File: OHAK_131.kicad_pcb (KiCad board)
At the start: 4 copper layers, 38.1 x 25.4 mm, 52 parts, among them P1 CONN_01X08, P2 USB_OTG, U1 rfd_77101, U2 MAX30100, U3 MIC5365-X.XYMT-TZ, U4 BMI160, U5 MCP73831, U6 MIC5365-X.XYMT-TZ, U7 TXS0102_LEVEL_SHIFTER_X2SON8, U8 MAX809

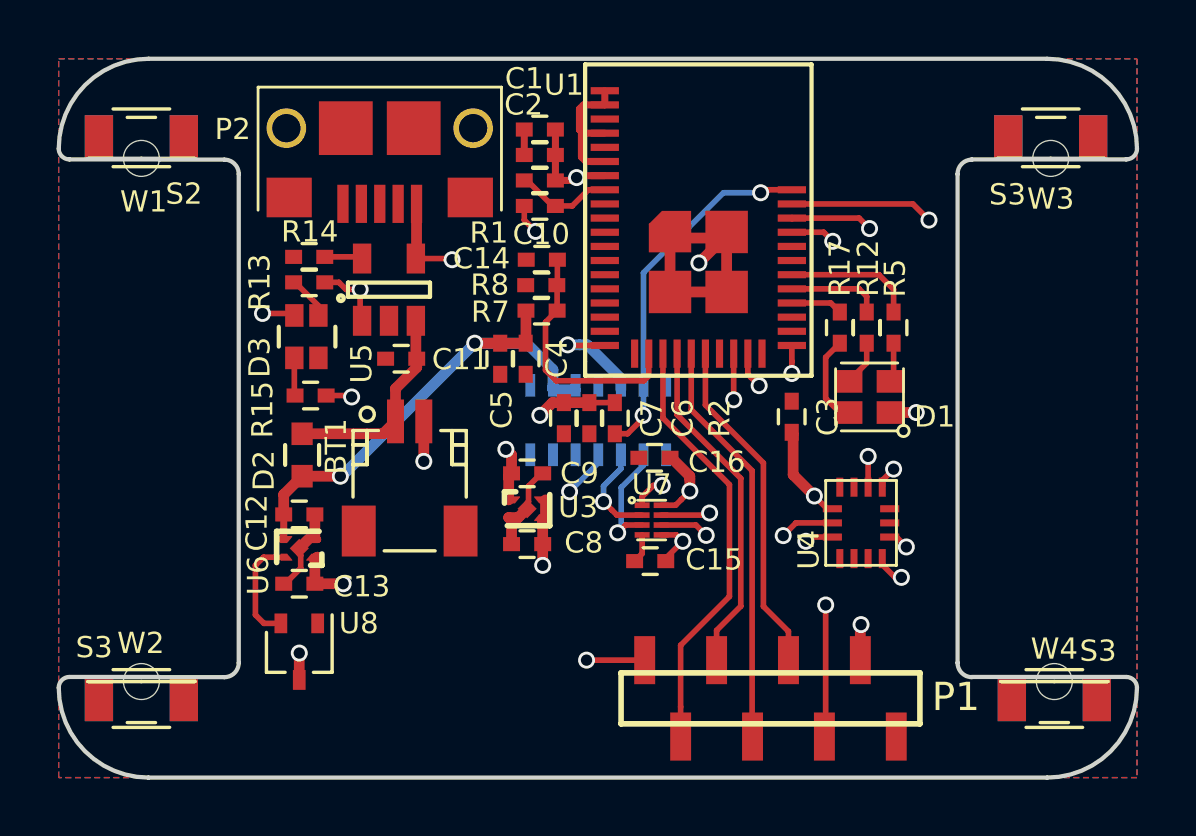
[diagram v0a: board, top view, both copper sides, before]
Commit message: fixed mis pinned part. moved stuff around
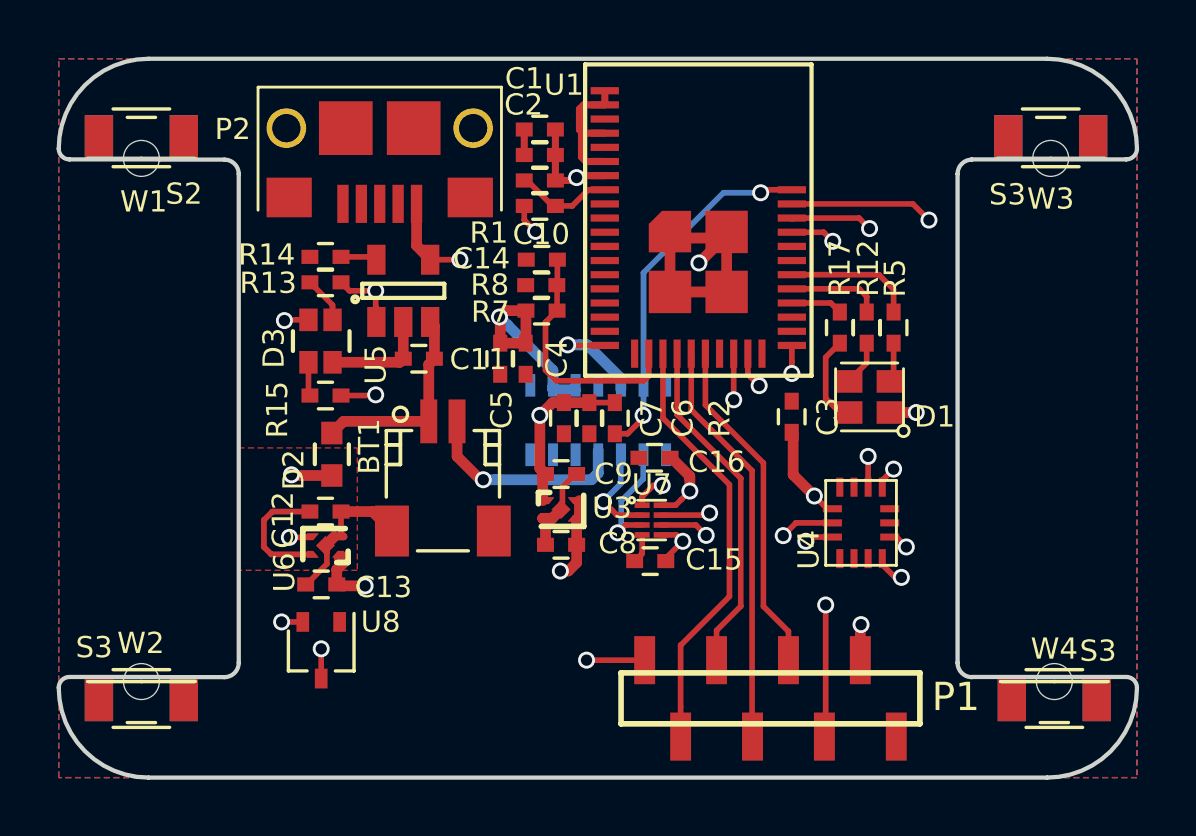
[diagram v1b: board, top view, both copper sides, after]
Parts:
- D1: value Led_RGB_CA -> ASMB-KTF0-0A306
- D3: value Dialight_R_G_LED -> 18-225SURSYGC/S530-A4/E4/TR8
- P1: value CONN_01X08 -> M50-3140845
- R12, R17: value 30R -> 100R
- R5: value 130R -> 100R
- U3: value MIC5365-X.XYMT-TZ -> MIC5365-1.8YMT-TZ
- U5: value MCP73831 -> MCP73831T-2ATI/OT
- U6: value MIC5365-X.XYMT-TZ -> MIC5365-3.0YMT-TZ
- U7: value TXS0102_LEVEL_SHIFTER_X2SON8 -> TXS0102DQER
- U8: value MAX809 -> MAX809SQ308T1G
- moved U3 1.20 mm to (139.1, 101.4)
- moved C8 1.20 mm to (139.1, 102.7)
- moved C9 1.20 mm to (139.1, 100.2)
- moved BT1 1.17 mm to (134.9, 100.2)
- moved D2 1.05 mm to (131.0, 99.5)
- moved C12 0.93 mm to (130.8, 101.5)
- moved U6 0.93 mm to (130.8, 102.7)
- moved U8 0.78 mm to (130.6, 106.4)
- moved C13 0.78 mm to (130.6, 104.1)
- moved C11 0.62 mm to (134.1, 96.1)
- moved R13 0.58 mm to (130.8, 93.4)
- moved R14 0.58 mm to (130.8, 92.5)
- moved R15 0.53 mm to (130.8, 97.4)
- moved D3 0.52 mm to (130.6, 95.5)
- moved U5 0.51 mm to (133.5, 93.7)
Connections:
- U6 pad 3: VPP -> /EN
- U6 pad 4: /EN -> VPP
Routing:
- net GND: track 33.4 -> 44.0 mm, vias 5 -> 4
- net VPP: track 26.1 -> 31.4 mm
- net +1V8: track 7.73 -> 8.96 mm, vias 4 -> 3
- net VDD: track 17.8 -> 18.9 mm
- net Net-(D3-Pad3): track 11.9 -> 11.2 mm
- net /EN: track 3.79 -> 4.49 mm, vias 0 -> 2
- added copper zone on F.Cu, net VPP

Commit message: FIXED BREAKS IN COPPER POURS
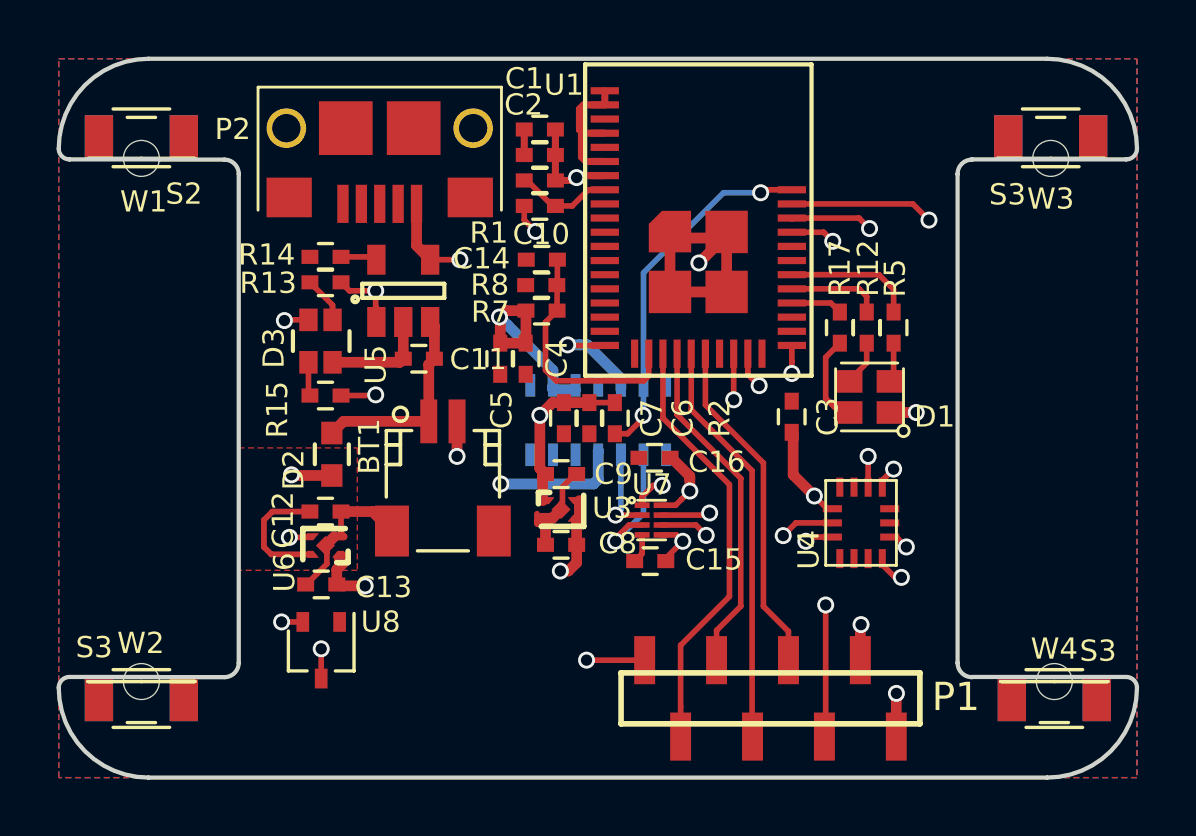
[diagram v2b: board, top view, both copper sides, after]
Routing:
- net GND: track 44.0 -> 44.6 mm, vias 4 -> 6
- net /1V8_SCL: track 4.26 -> 4.85 mm
- added copper zone on In1.Cu, net VPP
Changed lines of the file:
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@@
     (thickness 1.6)
     (drawings 54)
-    (tracks 349)
+    (tracks 352)
     (zones 0)
     (modules 52)
@@
     (33 F.Adhes user)
     (34 B.Paste user hide)
-    (35 F.Paste user)
+    (35 F.Paste user hide)
     (36 B.SilkS user hide)
-    (37 F.SilkS user)
+    (37 F.SilkS user hide)
     (38 B.Mask user hide)
     (39 F.Mask user hide)
@@
     (44 Edge.Cuts user)
     (45 Margin user)
-    (46 B.CrtYd user)
-    (47 F.CrtYd user)
+    (46 B.CrtYd user hide)
+    (47 F.CrtYd user hide)
     (48 B.Fab user hide)
     (49 F.Fab user hide)
@@
     (mod_text_size 0.75 0.75)
     (mod_text_width 0.15)
-    (pad_size 1.6 1.4)
+    (pad_size 1 1.6)
     (pad_drill 0)
     (pad_to_mask_clearance 0.2)
@@
   (segment (start 133.39088 96.21886) (end 133.51588 96.09386) (width 0.381) (layer F.Cu) (net 1))
   (segment (start 131.01588 96.21886) (end 133.39088 96.21886) (width 0.381) (layer F.Cu) (net 1))
-  (via (at 136.34088 100.36886) (size 0.6) (drill 0.4) (layers F.Cu B.Cu) (net 1))
-  (segment (start 136.765144 100.36886) (end 136.34088 100.36886) (width 0.381) (layer B.Cu) (net 1))
-  (segment (start 140.16588 100.36886) (end 136.765144 100.36886) (width 0.381) (layer B.Cu) (net 1))
-  (segment (start 140.40388 99.33686) (end 140.40388 100.13086) (width 0.381) (layer B.Cu) (net 1))
-  (segment (start 140.40388 100.13086) (end 140.16588 100.36886) (width 0.381) (layer B.Cu) (net 1))
-  (segment (start 135.41588 99.54386) (end 136.24088 100.36886) (width 0.381) (layer F.Cu) (net 1))
-  (segment (start 136.24088 100.36886) (end 136.34088 100.36886) (width 0.381) (layer F.Cu) (net 1))
-  (segment (start 135.41588 98.30636) (end 135.41588 99.54386) (width 0.381) (layer F.Cu) (net 1))
+  (segment (start 138.44088 101.731361) (end 138.303381 101.731361) (width 0.2032) (layer F.Cu) (net 1))
+  (segment (start 138.303381 101.731361) (end 138.26588 101.768862) (width 0.2032) (layer F.Cu) (net 1))
+  (segment (start 138.26588 101.768862) (end 138.26588 101.94386) (width 0.2032) (layer F.Cu) (net 1))
+  (segment (start 138.26588 101.94386) (end 138.24088 101.91886) (width 0.2032) (layer F.Cu) (net 1))
+  (segment (start 138.24088 101.91886) (end 138.24088 101.56886) (width 0.2032) (layer F.Cu) (net 1))
+  (segment (start 135.41588 99.54386) (end 135.41588 98.30636) (width 0.381) (layer F.Cu) (net 1))
+  (via (at 135.41588 99.54386) (size 0.6) (drill 0.4) (layers F.Cu B.Cu) (net 1))
+  (segment (start 140.41588 99.34886) (end 140.40388 99.33686) (width 0.381) (layer B.Cu) (net 1))
+  (segment (start 140.40388 99.33686) (end 140.40388 100.35586) (width 0.381) (layer B.Cu) (net 1))
+  (via (at 136.96588 100.51886) (size 0.6) (drill 0.4) (layers F.Cu B.Cu) (net 1))
+  (segment (start 140.24088 100.51886) (end 136.96588 100.51886) (width 0.381) (layer B.Cu) (net 1))
+  (segment (start 140.40388 100.35586) (end 140.24088 100.51886) (width 0.381) (layer B.Cu) (net 1))
+  (via (at 150.94088 107.91886) (size 0.6) (drill 0.4) (layers F.Cu B.Cu) (net 1))
+  (segment (start 150.93588 107.92386) (end 150.94088 107.91886) (width 0.381) (layer F.Cu) (net 1))
+  (segment (start 150.93588 109.44386) (end 150.93588 107.92386) (width 0.381) (layer F.Cu) (net 1))
   (segment (start 138.89088 87.99386) (end 138.89088 88.89386) (width 0.25) (layer F.Cu) (net 2))
   (segment (start 138.89088 89.79386) (end 138.89088 88.89386) (width 0.25) (layer F.Cu) (net 2))
@@
   (segment (start 129.59088 100.21886) (end 129.56588 100.19386) (width 0.381) (layer F.Cu) (net 24))
   (segment (start 130.99088 100.21886) (end 129.59088 100.21886) (width 0.381) (layer F.Cu) (net 24))
-  (segment (start 131.34088 100.19386) (end 136.91588 94.61886) (width 0.381) (layer In1.Cu) (net 24))
-  (segment (start 129.56588 100.19386) (end 131.34088 100.19386) (width 0.381) (layer In1.Cu) (net 24))
   (segment (start 130.61588 107.39386) (end 130.61588 106.343868) (width 0.2) (layer F.Cu) (net 24))
   (segment (start 128.85338 103.00636) (end 130.11588 103.00636) (width 0.2032) (layer F.Cu) (net 24))
@@
   (segment (start 130.615872 101.243852) (end 129.56588 100.19386) (width 0.2) (layer In2.Cu) (net 24))
   (segment (start 130.615872 106.34386) (end 130.615872 101.243852) (width 0.2) (layer In2.Cu) (net 24))
+  (segment (start 136.74088 94.61886) (end 136.91588 94.61886) (width 0.381) (layer In1.Cu) (net 24))
+  (segment (start 131.16588 100.19386) (end 136.74088 94.61886) (width 0.381) (layer In1.Cu) (net 24))
+  (segment (start 129.56588 100.19386) (end 131.16588 100.19386) (width 0.381) (layer In1.Cu) (net 24))
   (via (at 146.14398 90.22842) (size 0.6) (drill 0.4) (layers F.Cu B.Cu) (net 25))
   (segment (start 146.14398 90.22842) (end 146.24854 90.12386) (width 0.25) (layer F.Cu) (net 25))
@@
   (segment (start 130.16588 97.34386) (end 130.21588 97.39386) (width 0.2) (layer F.Cu) (net 50))
   (segment (start 130.16588 96.21886) (end 130.16588 97.34386) (width 0.2) (layer F.Cu) (net 50))
-  (via (at 141.09088 102.24386) (size 0.6) (drill 0.4) (layers F.Cu B.Cu) (net 51))
-  (segment (start 141.36588 101.96886) (end 141.09088 102.24386) (width 0.2) (layer F.Cu) (net 51))
-  (segment (start 141.95588 101.96886) (end 141.36588 101.96886) (width 0.2) (layer F.Cu) (net 51))
-  (segment (start 141.99088 100.34386) (end 141.99088 99.34986) (width 0.2) (layer B.Cu) (net 51))
-  (segment (start 141.21588 101.11886) (end 141.99088 100.34386) (width 0.2) (layer B.Cu) (net 51))
-  (segment (start 141.21588 102.11886) (end 141.21588 101.11886) (width 0.2) (layer B.Cu) (net 51))
-  (segment (start 141.99088 99.34986) (end 142.00388 99.33686) (width 0.2) (layer B.Cu) (net 51))
-  (segment (start 141.09088 102.24386) (end 141.21588 102.11886) (width 0.2) (layer B.Cu) (net 51))
+  (segment (start 141.49088 101.96886) (end 141.95588 101.96886) (width 0.2) (layer F.Cu) (net 51))
+  (segment (start 141.01588 102.54387) (end 141.01588 102.44386) (width 0.2) (layer F.Cu) (net 51))
+  (segment (start 141.01588 102.44386) (end 141.49088 101.96886) (width 0.2) (layer F.Cu) (net 51))
+  (segment (start 141.01588 102.54387) (end 142.00388 101.55587) (width 0.2) (layer B.Cu) (net 51))
+  (segment (start 142.00388 101.55587) (end 142.00388 99.33686) (width 0.2) (layer B.Cu) (net 51))
+  (via (at 141.01588 102.54387) (size 0.6) (drill 0.4) (layers F.Cu B.Cu) (net 51))
   (via (at 144.219234 102.334559) (size 0.6) (drill 0.4) (layers F.Cu B.Cu) (net 52))
   (segment (start 143.853535 101.96886) (end 142.62588 101.96886) (width 0.2) (layer F.Cu) (net 52))
@@
   (segment (start 144.228535 102.34386) (end 144.219234 102.334559) (width 0.2) (layer In1.Cu) (net 52))
   (segment (start 146.94088 102.34386) (end 144.228535 102.34386) (width 0.2) (layer In1.Cu) (net 52))
-  (segment (start 141.06588 101.61886) (end 140.890879 101.443859) (width 0.2) (layer F.Cu) (net 53))
-  (segment (start 140.890879 101.443859) (end 140.59088 101.14386) (width 0.2) (layer F.Cu) (net 53))
-  (segment (start 141.95588 101.61886) (end 141.06588 101.61886) (width 0.2) (layer F.Cu) (net 53))
-  (via (at 140.59088 101.14386) (size 0.6) (drill 0.4) (layers F.Cu B.Cu) (net 53))
-  (segment (start 140.59088 101.11886) (end 140.59088 101.14386) (width 0.2) (layer B.Cu) (net 53))
-  (segment (start 141.20388 100.50586) (end 140.59088 101.11886) (width 0.2) (layer B.Cu) (net 53))
-  (segment (start 141.20388 99.33686) (end 141.20388 100.50586) (width 0.2) (layer B.Cu) (net 53))
+  (segment (start 141.95588 101.61886) (end 141.015874 101.61886) (width 0.2) (layer F.Cu) (net 53))
+  (via (at 141.015874 101.61886) (size 0.6) (drill 0.4) (layers F.Cu B.Cu) (net 53))
+  (segment (start 141.20388 101.430854) (end 141.015874 101.61886) (width 0.2) (layer B.Cu) (net 53))
+  (segment (start 141.20388 99.33686) (end 141.20388 101.430854) (width 0.2) (layer B.Cu) (net 53))
   (via (at 144.34088 101.54386) (size 0.6) (drill 0.4) (layers F.Cu B.Cu) (net 54))
   (segment (start 144.26588 101.61886) (end 142.62588 101.61886) (width 0.2) (layer F.Cu) (net 54))
@@
     (polygon
       (pts
-        (xy 153.09088 90.82786) (xy 151.56688 90.82786) (xy 142.82888 90.82786) (xy 141.30488 89.30386) (xy 141.34088 85.49386)
-        (xy 153.09088 85.49386) (xy 153.09088 89.04986)
+        (xy 159.39088 90.81886) (xy 151.56688 90.82786) (xy 142.82888 90.82786) (xy 141.30488 89.30386) (xy 141.34088 85.49386)
+        (xy 159.44088 85.49386) (xy 159.39088 89.06886)
       )
     )
@@
     (priority 1)
     (connect_pads (clearance 0.2))
+    (min_thickness 0.254)
+    (fill yes (arc_segments 16) (thermal_gap 0.508) (thermal_bridge_width 0.508))
+    (polygon
+      (pts
+        (xy 127.69088 99.24386) (xy 131.89088 99.24386) (xy 131.89088 103.56886) (xy 127.71588 103.56886)
+      )
+    )
+  )
+  (zone (net 24) (net_name VPP) (layer In1.Cu) (hatch edge 0.508)
+    (priority 1)
+    (connect_pads (clearance 0.2))

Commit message: resixed solder mask aperature
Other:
- rule pad_to_mask_clearance: 0.2 -> 0.03
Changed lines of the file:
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@@
     (2 In2.Cu signal)
     (31 B.Cu signal)
-    (32 B.Adhes user)
-    (33 F.Adhes user)
-    (34 B.Paste user hide)
-    (35 F.Paste user hide)
-    (36 B.SilkS user hide)
-    (37 F.SilkS user hide)
-    (38 B.Mask user hide)
-    (39 F.Mask user hide)
+    (32 B.Adhes user hide)
+    (33 F.Adhes user hide)
+    (34 B.Paste user)
+    (35 F.Paste user)
+    (36 B.SilkS user)
+    (37 F.SilkS user)
+    (38 B.Mask user)
+    (39 F.Mask user)
     (40 Dwgs.User user hide)
     (41 Cmts.User user hide)
@@
   )
   (setup
-    (last_trace_width 0.381)
+    (last_trace_width 0.25)
     (user_trace_width 0.18)
     (user_trace_width 0.2)
@@
     (pad_size 1 1.6)
     (pad_drill 0)
-    (pad_to_mask_clearance 0.2)
+    (pad_to_mask_clearance 0.03)
     (solder_mask_min_width 0.25)
     (aux_axis_origin 121.34088 110.89386)
@@
     (add_net VDD)
   )
+  (module Solutions:LGA_2.5x3 (layer F.Cu)
+    (at 149.69088 101.89386 90)
+    (fp_text reference U4 (at -0.95 -1.85 90) (layer F.SilkS)
+      (effects (font (size 0.75 0.75) (thickness 0.15)))
+    )
+    (fp_text value BMI160 (at 0 2.5 90) (layer F.Fab)
+      (effects (font (size 0.75 0.75) (thickness 0.15)))
+    )
+    (fp_line (start -1.5 1.25) (end -1.5 -1.25) (layer F.SilkS) (width 0.1))
+    (fp_line (start 1.5 1.25) (end -1.5 1.25) (layer F.SilkS) (width 0.1))
+    (fp_line (start 1.5 -1.25) (end 1.5 1.25) (layer F.SilkS) (width 0.1))
+    (fp_line (start -1.5 -1.25) (end 1.5 -1.25) (layer F.SilkS) (width 0.1))
+    (pad 13 smd rect (at 0 -1.0125 90) (size 0.25 0.675) (layers F.Cu F.Paste F.Mask)
+      (net 52 /3V3_SCL))
+    (pad 1 smd rect (at -1.2625 -0.75 90) (size 0.675 0.25) (layers F.Cu F.Paste F.Mask)
+      (net 1 GND))
+    (pad 2 smd rect (at -1.2625 -0.25 90) (size 0.675 0.25) (layers F.Cu F.Paste F.Mask)
+      (net 31 "Net-(U4-Pad2)"))
+    (pad 3 smd rect (at -1.2625 0.25 90) (size 0.675 0.25) (layers F.Cu F.Paste F.Mask)
+      (net 30 "Net-(U4-Pad3)"))
+    (pad 4 smd rect (at -1.2625 0.75 90) (size 0.675 0.25) (layers F.Cu F.Paste F.Mask)
+      (net 29 /BMI_INT1))
+    (pad 8 smd rect (at 1.2625 0.75 90) (size 0.675 0.25) (layers F.Cu F.Paste F.Mask)
+      (net 2 VDD))
+    (pad 9 smd rect (at 1.2625 0.25 90) (size 0.675 0.25) (layers F.Cu F.Paste F.Mask)
+      (net 28 /BMI_INT2))
+    (pad 10 smd rect (at 1.2625 -0.25 90) (size 0.675 0.25) (layers F.Cu F.Paste F.Mask)
+      (net 27 "Net-(U4-Pad10)"))
+    (pad 11 smd rect (at 1.2625 -0.75 90) (size 0.675 0.25) (layers F.Cu F.Paste F.Mask)
+      (net 26 "Net-(U4-Pad11)"))
+    (pad 14 smd rect (at -0.5 -1.0125 90) (size 0.25 0.675) (layers F.Cu F.Paste F.Mask)
+      (net 54 /3V3_SDA))
+    (pad 12 smd rect (at 0.5 -1.0125 90) (size 0.25 0.675) (layers F.Cu F.Paste F.Mask)
+      (net 2 VDD))
+    (pad 7 smd rect (at 0.5 1.0125 90) (size 0.25 0.675) (layers F.Cu F.Paste F.Mask)
+      (net 1 GND))
+    (pad 6 smd rect (at 0 1.0125 90) (size 0.25 0.675) (layers F.Cu F.Paste F.Mask)
+      (net 1 GND))
+    (pad 5 smd rect (at -0.5 1.0125 90) (size 0.25 0.675) (layers F.Cu F.Paste F.Mask)
+      (net 2 VDD))
+  )
   (module Capacitors_SMD:C_0402 (layer F.Cu)
     (at 130.76588 101.49386 180)
@@
     )
   )
-  (module Solutions:LGA_2.5x3 (layer F.Cu)
-    (at 149.69088 101.89386 90)
-    (fp_text reference U4 (at -0.95 -1.85 90) (layer F.SilkS)
-      (effects (font (size 0.75 0.75) (thickness 0.15)))
-    )
-    (fp_text value BMI160 (at 0 2.5 90) (layer F.Fab)
-      (effects (font (size 0.75 0.75) (thickness 0.15)))
-    )
-    (fp_line (start -1.5 -1.25) (end 1.5 -1.25) (layer F.SilkS) (width 0.1))
-    (fp_line (start 1.5 -1.25) (end 1.5 1.25) (layer F.SilkS) (width 0.1))
-    (fp_line (start 1.5 1.25) (end -1.5 1.25) (layer F.SilkS) (width 0.1))
-    (fp_line (start -1.5 1.25) (end -1.5 -1.25) (layer F.SilkS) (width 0.1))
-    (pad 5 smd rect (at -0.5 1.0125 90) (size 0.25 0.675) (layers F.Cu F.Paste F.Mask)
-      (net 2 VDD))
-    (pad 6 smd rect (at 0 1.0125 90) (size 0.25 0.675) (layers F.Cu F.Paste F.Mask)
-      (net 1 GND))
-    (pad 7 smd rect (at 0.5 1.0125 90) (size 0.25 0.675) (layers F.Cu F.Paste F.Mask)
-      (net 1 GND))
-    (pad 12 smd rect (at 0.5 -1.0125 90) (size 0.25 0.675) (layers F.Cu F.Paste F.Mask)
-      (net 2 VDD))
-    (pad 14 smd rect (at -0.5 -1.0125 90) (size 0.25 0.675) (layers F.Cu F.Paste F.Mask)
-      (net 54 /3V3_SDA))
-    (pad 11 smd rect (at 1.2625 -0.75 90) (size 0.675 0.25) (layers F.Cu F.Paste F.Mask)
-      (net 26 "Net-(U4-Pad11)"))
-    (pad 10 smd rect (at 1.2625 -0.25 90) (size 0.675 0.25) (layers F.Cu F.Paste F.Mask)
-      (net 27 "Net-(U4-Pad10)"))
-    (pad 9 smd rect (at 1.2625 0.25 90) (size 0.675 0.25) (layers F.Cu F.Paste F.Mask)
-      (net 28 /BMI_INT2))
-    (pad 8 smd rect (at 1.2625 0.75 90) (size 0.675 0.25) (layers F.Cu F.Paste F.Mask)
-      (net 2 VDD))
-    (pad 4 smd rect (at -1.2625 0.75 90) (size 0.675 0.25) (layers F.Cu F.Paste F.Mask)
-      (net 29 /BMI_INT1))
-    (pad 3 smd rect (at -1.2625 0.25 90) (size 0.675 0.25) (layers F.Cu F.Paste F.Mask)
-      (net 30 "Net-(U4-Pad3)"))
-    (pad 2 smd rect (at -1.2625 -0.25 90) (size 0.675 0.25) (layers F.Cu F.Paste F.Mask)
-      (net 31 "Net-(U4-Pad2)"))
-    (pad 1 smd rect (at -1.2625 -0.75 90) (size 0.675 0.25) (layers F.Cu F.Paste F.Mask)
-      (net 1 GND))
-    (pad 13 smd rect (at 0 -1.0125 90) (size 0.25 0.675) (layers F.Cu F.Paste F.Mask)
-      (net 52 /3V3_SCL))
-  )
   (module Solutions:0606_Bi-Color (layer F.Cu)
